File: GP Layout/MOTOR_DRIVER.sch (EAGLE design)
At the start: 29 parts, among them U1 CSD18502KCS_KCS_3, U2 CSD18502KCS_KCS_3, U3 MIC4604YM, U4 CSD18502KCS_KCS_3, U5 CSD18502KCS_KCS_3, U6 MIC4604YM, U7 ATMEGA328P_TQFP, Y1 16MHz

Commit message: Updated all schematic sheets
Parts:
- added D3, D4: BYV32, diode:BYV32
- added S1: SWS006, smd-special:SWS006
- C7: value (none) -> 10uF
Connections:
- removed net M2_GPIO1: JP5.10, U$1.19/A5/SCL
- removed net M2_GPIO2: JP5.12, U$1.18/A4/SDA
- removed net M2_GPIO3: JP5.14, U$1.A22/DAC1
- removed net M2_GPIO4: JP5.16, U$1.A21/DAC0
- removed net M2_GPIO5: JP5.18, U$1.39/A20
- removed net RECEIVER: JP5.20, U$1.5
- removed net SWITCHES: U$1.33/A14, U$1.34/A15, U$1.35/A16, U$1.36/A17
- new net 5V_TEENSY: S1.6, U$1.VIN
- new net 7_4V1: D4.A1, D4.A2
- new net N$14: D4.C
- new net N$17: LSP1.MP
- new net REC_MOTOR: JP5.20, U$1.15/A1
- new net REC_SERVO: U$1.18/A4/SDA
- new net SW1: S1.1, U$1.24
- new net SW2: S1.2, U$1.25
- new net SW3: S1.3, U$1.26
- new net SW4: S1.4, U$1.27
- new net SW5: S1.5, U$1.28
- net 5V: now also S1.7; no longer U$1.VIN
- net 7_4V: now also D3.A1, D3.A2; no longer LSP1.MP, U$2.VIN
- net BLT_RX: now also U$1.7; no longer U$1.0/RX
- net BLT_TX: now also U$1.8; no longer U$1.1/TX
- net GND: now also S1.10, S1.11, S1.12, S1.8, S1.9
- net HALL: now also U7.PD2(INT0); no longer U7.PB1(OC1A)
- net M1_GPIO3: now also U7.PB1(OC1A); no longer U7.PD2(INT0)
- net N$5: now also D3.C
- net SERVO: now also U$1.20/A6; no longer U$1.16/A2
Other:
- moved on the sheet: C7

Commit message: Multilevel design
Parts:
- removed JP1: (no value), pinhead:PINHD-1X4
- removed JP2, JP4: (no value), pinhead:PINHD-1X3
- removed JP3: (no value), pinhead:PINHD-1X2
- removed JP5: (no value), pinhead:PINHD-2X10
- removed R1: 10k, resistor:R-US_0204/7
- added SV1, SV2, SV3, SV4, SV5, SV6, SV7, SV8: (no value), con-lsta:FE10-1
- renumbered U1 to TOP_FWD
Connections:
- removed net 7_4V1: D4.A1, D4.A2
- removed net N$14: D4.C
- removed net N$17: LSP1.MP
- new net 7_4V_TOP: D3.A1, D3.A2, D4.A1, D4.A2, LSP1.MP, SV5.1, TOP_FWD.DRAIN, U3.VDD, U4.DRAIN, U6.VDD
- new net GND_TOP: D1.A1, D1.A2, D2.A1, D2.A2, LSP2.MP, SV5.10, U2.SOURCE, U3.VSS, U5.SOURCE, U6.VSS
- new net HI_TOP: SV6.1, U3.HI, U6.LI
- new net LI_TOP: SV6.2, U3.LI, U6.HI
- net 3_3V: no longer JP5.3, JP5.4
- net 5V: no longer JP1.4, JP2.2, JP4.2, JP5.1, JP5.2, R1.1
- net 7_4V: now also SV1.1, U$2.VIN; no longer D3.A1, D3.A2, JP5.6, TOP_FWD.DRAIN, U3.VDD, U4.DRAIN, U6.VDD
- net BLT_RX: no longer JP1.1
- net BLT_TX: no longer JP1.2
- net CAMERA_A0: no longer JP5.7
- net CAMERA_CLK: no longer JP5.11
- net CAMERA_SI: no longer JP5.9
- net GND: now also SV1.10; no longer D1.A1, D1.A2, D2.A1, D2.A2, JP1.3, JP2.3, JP4.1, JP5.5, JP5.8, LSP2.MP, U2.SOURCE, U3.VSS, U5.SOURCE, U6.VSS
- net HALL: no longer JP2.1, R1.2
- net HI: now also SV2.1; no longer U3.HI, U6.LI
- net LI: now also SV2.2; no longer U3.LI, U6.HI
- net M1_GPIO1: no longer JP5.13
- net M1_GPIO2: no longer JP5.15
- net M1_GPIO3: no longer JP5.17
- net M1_GPIO4: no longer JP5.19
- net N$12: now also D4.C
- net REC_MOTOR: no longer JP5.20
- net RX: no longer JP3.1
- net SERVO: no longer JP4.3
- net TX: no longer JP3.2
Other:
- note added: "Bottom left headers"
- note added: "Bottom right headers"
- note added: "Top left headers"
- note added: "Top right headers"
- note removed: "Bluetooth Headers"
- note removed: "Serial and Hall Headers"
- note removed: "Servo Headers"

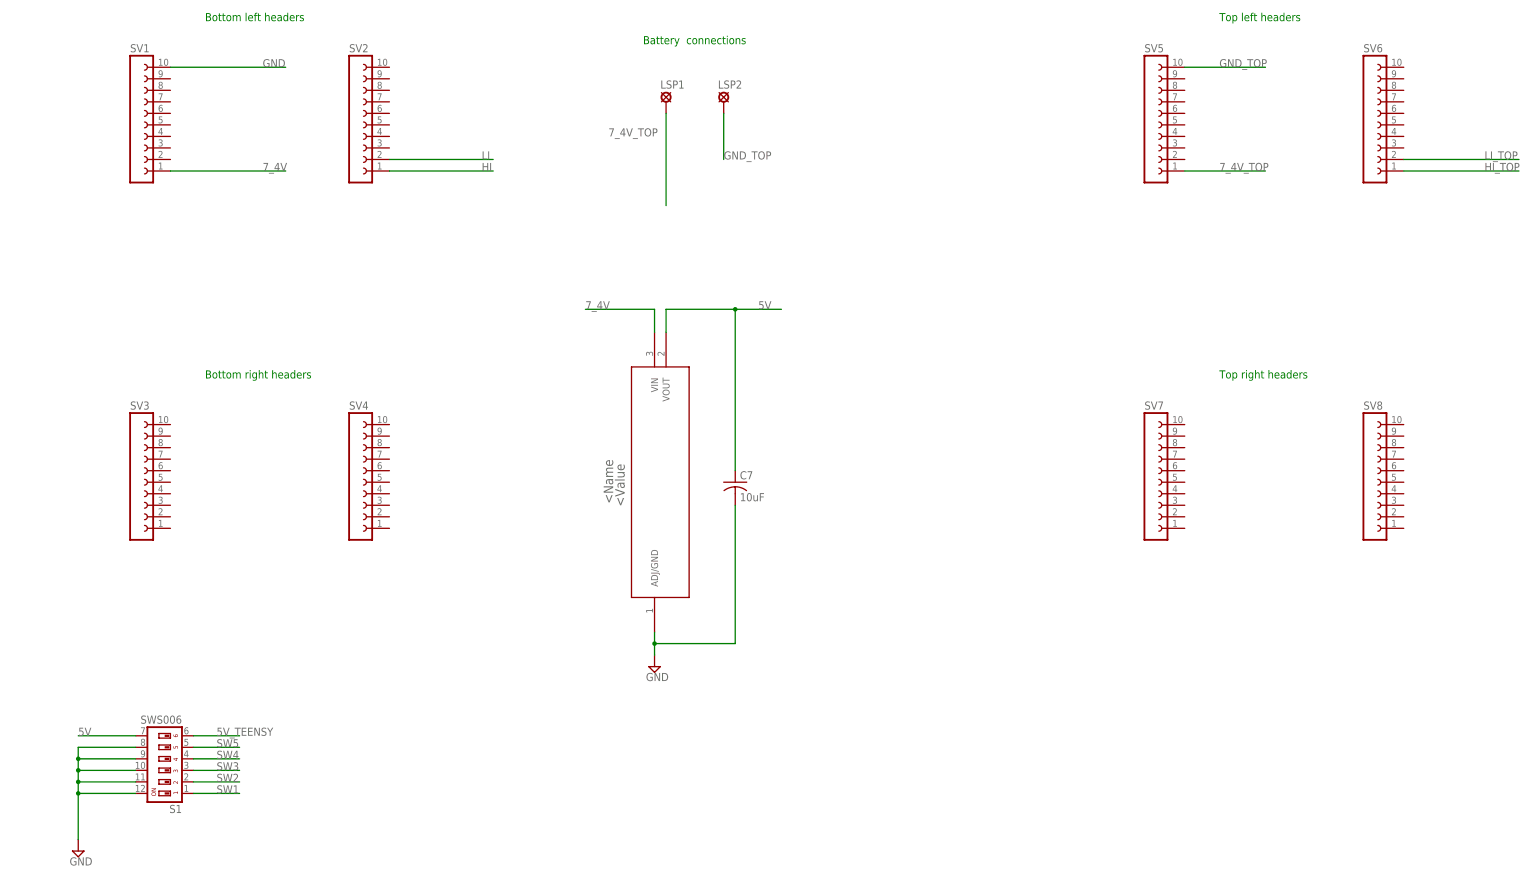
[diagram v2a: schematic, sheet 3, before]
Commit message: component placement
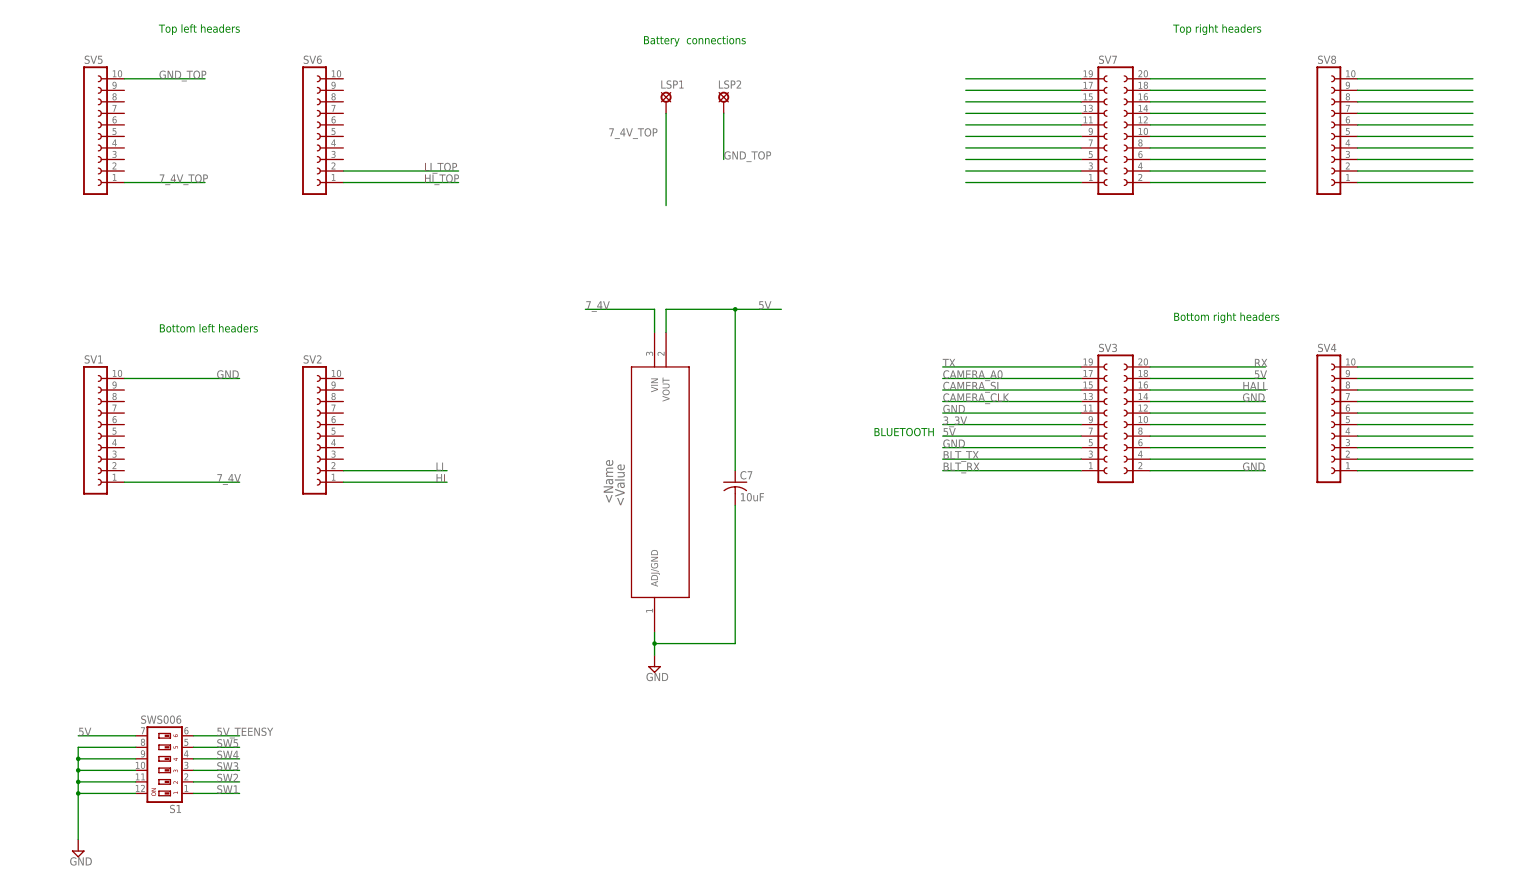
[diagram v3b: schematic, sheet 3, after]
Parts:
- SV3, SV7: device con-lsta:FE10-1 -> con-lsta:FE10-2
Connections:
- new net N$27: SV3.12
- net 3_3V: now also SV3.9
- net 5V: now also SV3.18, SV3.7
- net BLT_RX: now also SV3.1
- net BLT_TX: now also SV3.3
- net CAMERA_A0: now also SV3.17
- net CAMERA_CLK: now also SV3.13
- net CAMERA_SI: now also SV3.15
- net GND: now also SV3.11, SV3.14, SV3.5
- net HALL: now also SV3.16
- net RX: now also SV3.20
- net TX: now also SV3.19
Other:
- note added: "BLUETOOTH"
- moved on the sheet: SV1, SV2, SV4, SV5, SV6, SV8

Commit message: 2 level design - incomplete
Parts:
- removed D1, D2: BYV32, diode:BYV32
- removed LSP1, LSP2: SE14, solpad:SE14
- removed SV7: (no value), con-lsta:FE10-2
- removed SV8: (no value), con-lsta:FE10-1
- removed U$2: LM1086IT-5.0/NOPB, TI1086:LM1086IT-5.0/NOPB
- added C10, C11, C9: (no value), resistor:CPOL-US153CLV-1010
- added C8: 10uF, resistor:C-US050-025X075
- added LSP4, LSP5: SE14, solpad:SE14
- added U$3: LM1086IT-5.0/NOPB, TI1086:LM1086IT-5.0/NOPB
- C7: value 10uF -> (none); device resistor:C-US050-025X075 -> resistor:CPOL-US153CLV-1010
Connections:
- removed net N$27: SV3.12
- new net N$14: C10.-, C11.+
- new net N$17: C10.+, C9.-
- new net N$19: C7.-, C9.+
- new net N$20: SV3.4
- new net N$33: SV4.10
- new net N$34: SV4.9
- new net N$35: SV4.8
- new net N$36: SV4.7
- new net N$37: SV4.6
- new net N$38: SV4.5
- new net N$39: SV4.4
- new net N$40: SV4.3
- new net N$41: SV4.2
- new net N$42: SV4.1
- net 5V: now also C8.1, U$3.VOUT; no longer C7.1, U$2.VOUT
- net 7_4V: now also U$3.VIN; no longer U$2.VIN
- net 7_4V_TOP: now also LSP4.MP; no longer LSP1.MP
- net GND: now also C8.2, SV3.12, U$3.ADJ/GND; no longer C7.2, SV1.10, U$2.ADJ/GND
- net GND_TOP: now also C11.-, LSP5.MP; no longer D1.A1, D1.A2, D2.A1, D2.A2, LSP2.MP
- net N$1: no longer D2.C
- net N$8: no longer D1.C
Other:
- note removed: "Top right headers"

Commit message: Changed to two schematic sheets
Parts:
- removed C10, C11, C7, C9: (no value), resistor:CPOL-US153CLV-1010
- removed C8: 10uF, resistor:C-US050-025X075
- removed LSP4, LSP5: SE14, solpad:SE14
- removed S1: SWS006, smd-special:SWS006
- removed SV1, SV2, SV4, SV5, SV6: (no value), con-lsta:FE10-1
- removed SV3: (no value), con-lsta:FE10-2
- removed U$3: LM1086IT-5.0/NOPB, TI1086:LM1086IT-5.0/NOPB
- added C12: 10uF, resistor:C-US050-025X075
- added C13, C14, C15, C16: (no value), resistor:CPOL-US153CLV-1010
- added LSP1, LSP2: SE14, solpad:SE14
- added S2: SWS006, smd-special:SWS006
- added SV10, SV11, SV7, SV8, SV9: (no value), con-lsta:FE10-1
- added SV12: (no value), con-lsta:FE10-2
- added U$2: LM1086IT-5.0/NOPB, TI1086:LM1086IT-5.0/NOPB
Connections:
- removed net N$14: C10.-, C11.+
- removed net N$17: C10.+, C9.-
- removed net N$19: C7.-, C9.+
- removed net N$20: SV3.4
- removed net N$33: SV4.10
- removed net N$34: SV4.9
- removed net N$35: SV4.8
- removed net N$36: SV4.7
- removed net N$37: SV4.6
- removed net N$38: SV4.5
- removed net N$39: SV4.4
- removed net N$40: SV4.3
- removed net N$41: SV4.2
- removed net N$42: SV4.1
- new net N$21: C15.-, C16.+
- new net N$22: C14.-, C15.+
- new net N$23: C13.-, C14.+
- new net N$25: SV9.10
- new net N$26: SV9.9
- new net N$27: SV9.8
- new net N$28: SV9.7
- new net N$29: SV9.6
- new net N$30: SV9.5
- new net N$31: SV9.4
- new net N$32: SV9.3
- new net N$43: SV9.2
- new net N$44: SV9.1
- new net N$45: SV12.4
- net 3_3V: now also SV12.9; no longer SV3.9
- net 5V: now also C12.1, S2.7, SV12.18, SV12.7, U$2.VOUT; no longer C8.1, S1.7, SV3.18, SV3.7, U$3.VOUT
- net 5V_TEENSY: now also S2.6; no longer S1.6
- net 7_4V: now also SV7.1, U$2.VIN; no longer SV1.1, U$3.VIN
- net 7_4V_TOP: now also LSP1.MP, SV10.1; no longer LSP4.MP, SV5.1
- net BLT_RX: now also SV12.1; no longer SV3.1
- net BLT_TX: now also SV12.3; no longer SV3.3
- net CAMERA_A0: now also SV12.17; no longer SV3.17
- net CAMERA_CLK: now also SV12.13; no longer SV3.13
- net CAMERA_SI: now also SV12.15; no longer SV3.15
- net GND: now also C12.2, S2.10, S2.11, S2.12, S2.8, S2.9, SV12.11, SV12.12, SV12.14, SV12.5, U$2.ADJ/GND; no longer C8.2, S1.10, S1.11, S1.12, S1.8, S1.9, SV3.11, SV3.12, SV3.14, SV3.5, U$3.ADJ/GND
- net GND_TOP: now also C16.-, LSP2.MP, SV10.10; no longer C11.-, LSP5.MP, SV5.10
- net HALL: now also SV12.16; no longer SV3.16
- net HI: now also SV8.1; no longer SV2.1
- net HI_TOP: now also SV11.1; no longer SV6.1
- net LI: now also SV8.2; no longer SV2.2
- net LI_TOP: now also SV11.2; no longer SV6.2
- net RX: now also SV12.20; no longer SV3.20
- net SW1: now also S2.1; no longer S1.1
- net SW2: now also S2.2; no longer S1.2
- net SW3: now also S2.3; no longer S1.3
- net SW4: now also S2.4; no longer S1.4
- net SW5: now also S2.5; no longer S1.5
- net TX: now also SV12.19; no longer SV3.19

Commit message: Actual 4 schematic sheet update
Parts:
- removed C12: 10uF, resistor:C-US050-025X075
- removed C13, C14, C15, C16: (no value), resistor:CPOL-US153CLV-1010
- removed LSP1, LSP2: SE14, solpad:SE14
- removed S2: SWS006, smd-special:SWS006
- removed SV10, SV11, SV7, SV8, SV9: (no value), con-lsta:FE10-1
- removed SV12: (no value), con-lsta:FE10-2
- removed U$2: LM1086IT-5.0/NOPB, TI1086:LM1086IT-5.0/NOPB
- added C10, C11, C7, C9: (no value), resistor:CPOL-US153CLV-1010
- added C8: 10uF, resistor:C-US050-025X075
- added LSP4, LSP5: SE14, solpad:SE14
- added S1: SWS006, smd-special:SWS006
- added SV1, SV2, SV4, SV5, SV6: (no value), con-lsta:FE10-1
- added SV3: (no value), con-lsta:FE10-2
- added U$3: LM1086IT-5.0/NOPB, TI1086:LM1086IT-5.0/NOPB
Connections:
- removed net N$21: C15.-, C16.+
- removed net N$22: C14.-, C15.+
- removed net N$23: C13.-, C14.+
- removed net N$25: SV9.10
- removed net N$26: SV9.9
- removed net N$27: SV9.8
- removed net N$28: SV9.7
- removed net N$29: SV9.6
- removed net N$30: SV9.5
- removed net N$31: SV9.4
- removed net N$32: SV9.3
- removed net N$43: SV9.2
- removed net N$44: SV9.1
- removed net N$45: SV12.4
- new net N$14: C10.-, C11.+
- new net N$17: C10.+, C9.-
- new net N$19: C7.-, C9.+
- new net N$20: SV3.4
- new net N$33: SV4.10
- new net N$34: SV4.9
- new net N$35: SV4.8
- new net N$36: SV4.7
- new net N$37: SV4.6
- new net N$38: SV4.5
- new net N$39: SV4.4
- new net N$40: SV4.3
- new net N$41: SV4.2
- new net N$42: SV4.1
- net 3_3V: now also SV3.9; no longer SV12.9
- net 5V: now also C8.1, S1.7, SV3.18, SV3.6, SV3.7, U$3.VOUT; no longer C12.1, S2.7, SV12.18, SV12.7, U$2.VOUT
- net 5V_TEENSY: now also S1.6; no longer S2.6
- net 7_4V: now also SV1.1, U$3.VIN; no longer SV7.1, U$2.VIN
- net 7_4V_TOP: now also LSP4.MP, SV5.1; no longer LSP1.MP, SV10.1
- net BLT_RX: now also SV3.1; no longer SV12.1
- net BLT_TX: now also SV3.3; no longer SV12.3
- net CAMERA_A0: now also SV3.17; no longer SV12.17
- net CAMERA_CLK: now also SV3.13; no longer SV12.13
- net CAMERA_SI: now also SV3.15; no longer SV12.15
- net GND: now also C8.2, S1.10, S1.11, S1.12, S1.8, S1.9, SV3.11, SV3.12, SV3.14, SV3.2, SV3.5, U$3.ADJ/GND; no longer C12.2, S2.10, S2.11, S2.12, S2.8, S2.9, SV12.11, SV12.12, SV12.14, SV12.5, U$2.ADJ/GND
- net GND_TOP: now also C11.-, LSP5.MP, SV5.10; no longer C16.-, LSP2.MP, SV10.10
- net HALL: now also SV3.16; no longer SV12.16
- net HI: now also SV2.1; no longer SV8.1
- net HI_TOP: now also SV6.1; no longer SV11.1
- net LI: now also SV2.2; no longer SV8.2
- net LI_TOP: now also SV6.2; no longer SV11.2
- net REC_MOTOR: now also SV3.8
- net REC_SERVO: now also SV3.10
- net RX: now also SV3.20; no longer SV12.20
- net SW1: now also S1.1; no longer S2.1
- net SW2: now also S1.2; no longer S2.2
- net SW3: now also S1.3; no longer S2.3
- net SW4: now also S1.4; no longer S2.4
- net SW5: now also S1.5; no longer S2.5
- net TX: now also SV3.19; no longer SV12.19
